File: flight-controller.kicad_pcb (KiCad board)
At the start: 2 copper layers, 35 x 43 mm, 16 parts, among them J1 USB_C_Receptacle_USB2.0_16P, SW1 SW_Push, U1 ESP32-C3-WROOM-02, U2 MPU-6050, U3 AMS1117-3.3

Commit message: Improvements to schematics and PCB design. - GND always points down - Power always points up - Adjusted powerlines
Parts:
- moved R1 1.48 mm to (208.0, 73.5)
- moved R2 1.48 mm to (208.0, 75.5)
- moved J1 1.48 mm to (200.7, 75.3)
- moved R3 0.62 mm to (178.8, 57.9), turned to 90 degrees
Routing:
- net +3.3V: track 70.7 -> 73.2 mm
- net Net-(U1-EN): track 39.6 -> 37.6 mm, vias 4 -> 2
- net +5V: track 48.0 -> 49.5 mm
- net /USB_D-: track 42.9 -> 43.6 mm
- net /USB_D+: track 42.9 -> 43.6 mm

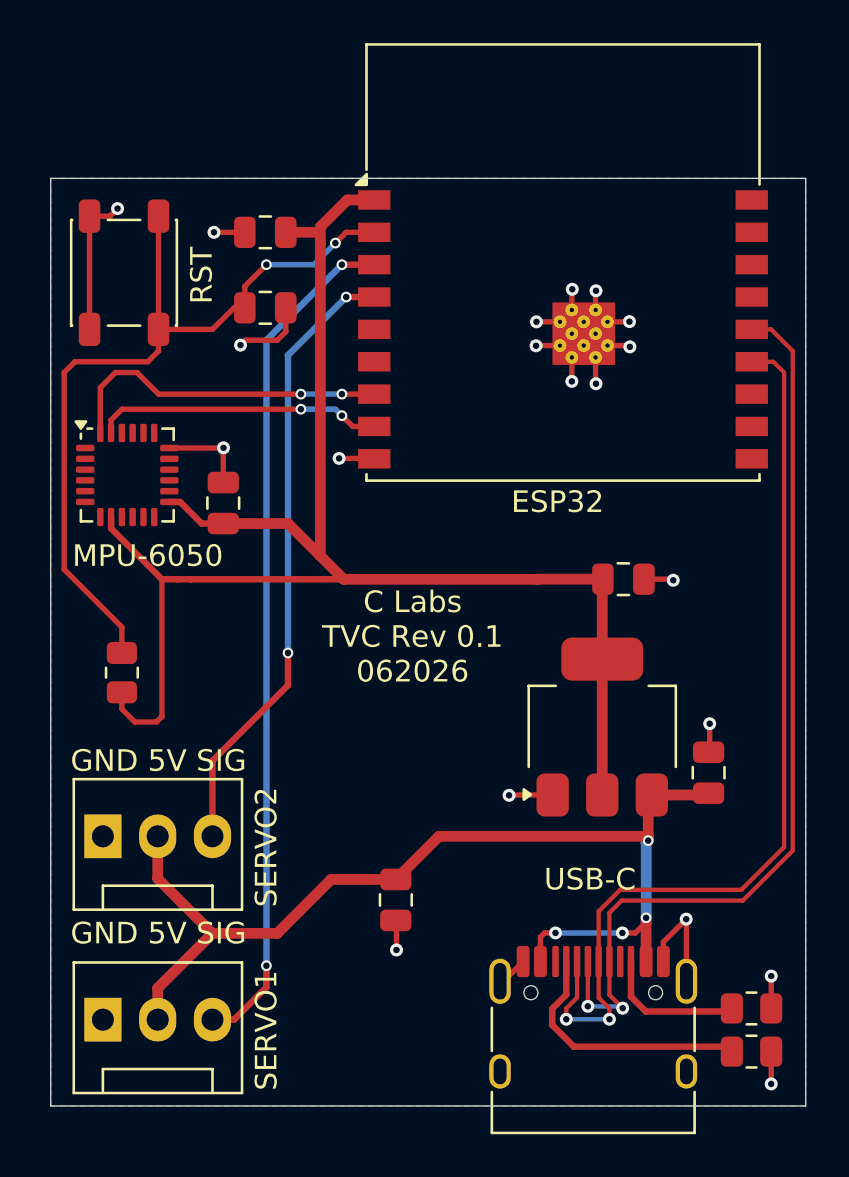
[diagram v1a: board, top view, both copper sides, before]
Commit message: Restructued Layout slightly and added new BOM
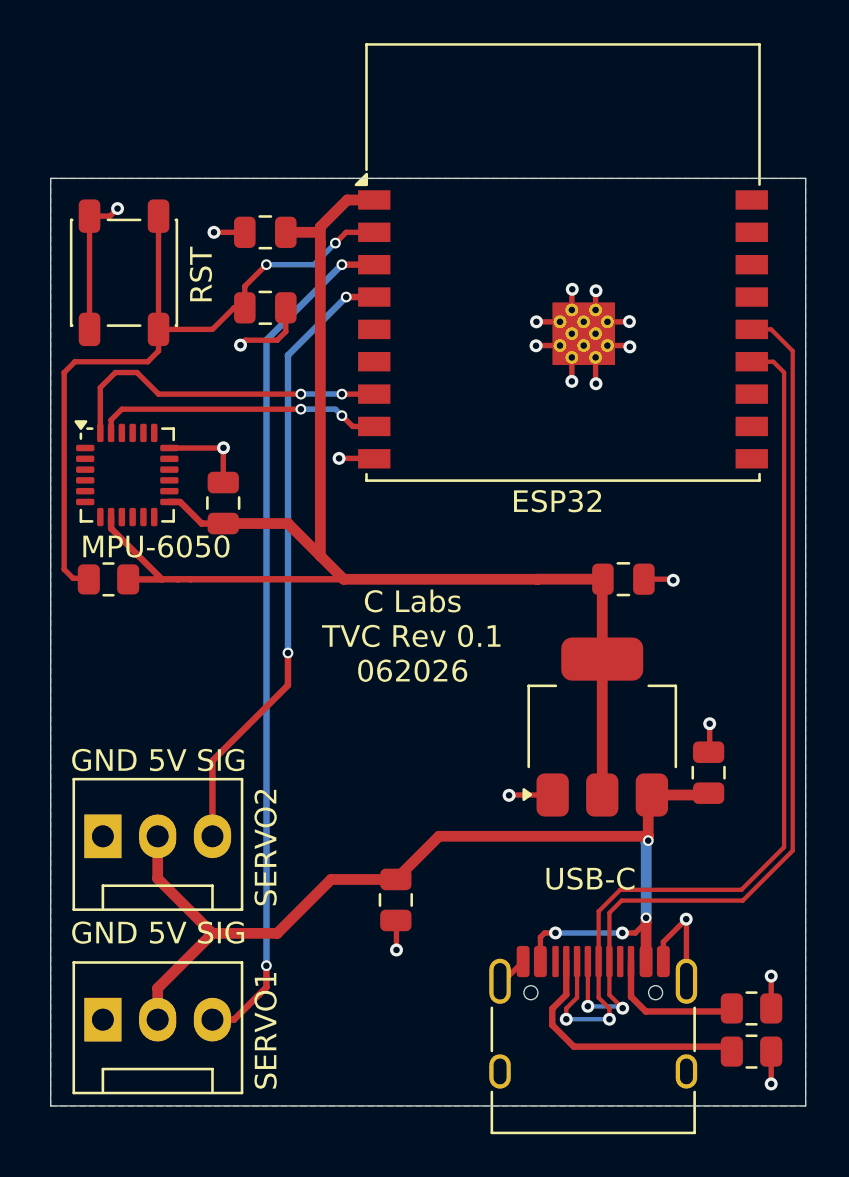
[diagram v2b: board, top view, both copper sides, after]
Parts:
- moved R3 4.37 mm to (178.2, 53.6), turned to 180 degrees
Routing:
- net +3.3V: track 73.2 -> 65.4 mm
- net Net-(U1-EN): track 37.6 -> 33.9 mm
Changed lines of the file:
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@@
 		(capping no)
 		(filling no)
-		(zone_defaults)
 		(pcbplotparams
 			(layerselection 0x00000000_00000000_55555555_5755f5ff)
@@
 		(sheetname "/")
 		(sheetfile "flight-controller.kicad_sch")
-		(units
-			(unit
-				(name "A")
-				(pins "2" "18" "17" "16" "15" "3" "4" "5" "6" "7" "8" "10" "13" "14"
-					"1" "9" "19" "11" "12"
-				)
-			)
-		)
 		(attr smd)
 		(duplicate_pad_numbers_are_jumpers no)
@@
 			(at -0.14 -0.35)
 			(size 0.6 0.6)
-			(drill 0.2)
+			(drill 0.3)
 			(property pad_prop_heatsink)
 			(layers "*.Cu" "F.Mask")
@@
 			(at -0.14 0.75)
 			(size 0.6 0.6)
-			(drill 0.2)
+			(drill 0.3)
 			(property pad_prop_heatsink)
 			(layers "*.Cu" "F.Mask")
@@
 			(at 0.41 -0.9)
 			(size 0.6 0.6)
-			(drill 0.2)
+			(drill 0.3)
 			(property pad_prop_heatsink)
 			(layers "*.Cu" "F.Mask")
@@
 			(at 0.41 0.2)
 			(size 0.6 0.6)
-			(drill 0.2)
+			(drill 0.3)
 			(property pad_prop_heatsink)
 			(layers "*.Cu" "F.Mask")
@@
 			(at 0.41 1.3)
 			(size 0.6 0.6)
-			(drill 0.2)
+			(drill 0.3)
 			(property pad_prop_heatsink)
 			(layers "*.Cu" "F.Mask")
@@
 			(at 0.96 -0.35)
 			(size 0.6 0.6)
-			(drill 0.2)
+			(drill 0.3)
 			(property pad_prop_heatsink)
 			(layers "*.Cu" "F.Mask")
@@
 			(at 0.96 0.75)
 			(size 0.6 0.6)
-			(drill 0.2)
+			(drill 0.3)
 			(property pad_prop_heatsink)
 			(layers "*.Cu" "F.Mask")
@@
 			(at 1.51 -0.9)
 			(size 0.6 0.6)
-			(drill 0.2)
+			(drill 0.3)
 			(property pad_prop_heatsink)
 			(layers "*.Cu" "F.Mask")
@@
 			(at 1.51 0.2)
 			(size 0.6 0.6)
-			(drill 0.2)
+			(drill 0.3)
 			(property pad_prop_heatsink)
 			(layers "*.Cu" "F.Mask")
@@
 			(at 1.51 1.3)
 			(size 0.6 0.6)
-			(drill 0.2)
+			(drill 0.3)
 			(property pad_prop_heatsink)
 			(layers "*.Cu" "F.Mask")
@@
 			(at 2.06 -0.35)
 			(size 0.6 0.6)
-			(drill 0.2)
+			(drill 0.3)
 			(property pad_prop_heatsink)
 			(layers "*.Cu" "F.Mask")
@@
 			(at 2.06 0.75)
 			(size 0.6 0.6)
-			(drill 0.2)
+			(drill 0.3)
 			(property pad_prop_heatsink)
 			(layers "*.Cu" "F.Mask")
@@
 	(footprint "Resistor_SMD:R_0805_2012Metric"
 		(layer "F.Cu")
-		(at 178.8 57.9125 90)
+		(at 178.18 53.59 180)
 		(descr "Resistor SMD 0805 (2012 Metric), square (rectangular) end terminal, IPC-7351 nominal, (Body size source: IPC-SM-782 page 72, https://www.pcb-3d.com/wordpress/wp-content/uploads/ipc-sm-782a_amendment_1_and_2.pdf)")
 		(tags "resistor")
 		(property "Reference" "R3"
-			(at 0 -1.65 90)
+			(at 0 -1.65 0)
 			(layer "F.SilkS")
 			(hide yes)
@@
 		)
 		(property "Value" "10k"
-			(at 0 1.65 90)
+			(at 0 1.65 0)
 			(layer "F.Fab")
 			(hide yes)
@@
 		)
 		(property "Datasheet" ""
-			(at 0 0 90)
+			(at 0 0 0)
 			(layer "F.Fab")
 			(hide yes)
@@
 		)
 		(property "Description" "Resistor"
-			(at 0 0 90)
+			(at 0 0 0)
 			(layer "F.Fab")
 			(hide yes)
@@
 		)
 		(property "KiLib_Generator" "SMD_2terminal_chip_molded"
-			(at 0 0 90)
+			(at 0 0 0)
 			(layer "F.SilkS")
 			(hide yes)
@@
 		(duplicate_pad_numbers_are_jumpers no)
 		(fp_line
-			(start -0.227064 -0.735)
-			(end 0.227064 -0.735)
+			(start -0.227064 0.735)
+			(end 0.227064 0.735)
 			(stroke
 				(width 0.12)
@@
 		)
 		(fp_line
-			(start -0.227064 0.735)
-			(end 0.227064 0.735)
+			(start -0.227064 -0.735)
+			(end 0.227064 -0.735)
 			(stroke
 				(width 0.12)
@@
 		)
 		(fp_text user "${REFERENCE}"
-			(at 0 0 90)
+			(at 0 0 0)
 			(layer "F.Fab")
 			(effects
@@
 		)
 		(fp_text user "${REFERENCE}"
-			(at 0 0 90)
+			(at 0 0 0)
 			(layer "F.Fab")
 			(effects
@@
 		)
 		(pad "1" smd roundrect
-			(at -0.9125 0 90)
+			(at -0.9125 0 180)
 			(size 1.025 1.4)
 			(layers "F.Cu" "F.Mask" "F.Paste")
@@
 		)
 		(pad "2" smd roundrect
-			(at 0.9125 0 90)
+			(at 0.9125 0 180)
 			(size 1.025 1.4)
 			(layers "F.Cu" "F.Mask" "F.Paste")
@@
 	)
 	(gr_text "MPU-6050\n"
-		(at 180 52.5 0)
+		(at 180.38 52.1 0)
 		(layer "F.SilkS")
 		(effects
@@
 	)
 	(segment
+		(start 180.65188 53.59)
+		(end 180.65688 53.585)
+		(width 0.25)
+		(layer "F.Cu")
+		(net "+3.3V")
+	)
+	(segment
 		(start 201.07 57.285)
 		(end 201.07 53.61)
@@
 	)
 	(segment
+		(start 179.0925 53.59)
+		(end 180.65188 53.59)
+		(width 0.3)
+		(layer "F.Cu")
+		(net "+3.3V")
+	)
+	(segment
 		(start 189.25 36)
 		(end 190.5 36)
@@
 	)
 	(segment
-		(start 180.4 60.2)
-		(end 179.4 60.2)
-		(width 0.25)
-		(layer "F.Cu")
-		(net "+3.3V")
-	)
-	(segment
 		(start 198.07 53.585)
 		(end 189.085 53.585)
@@
 	)
 	(segment
-		(start 178.8 59.6)
-		(end 178.8 58.825)
-		(width 0.25)
-		(layer "F.Cu")
-		(net "+3.3V")
-	)
-	(segment
 		(start 180.65688 53.585)
 		(end 181.4 53.585)
@@
 	)
 	(segment
-		(start 179.4 60.2)
-		(end 178.8 59.6)
-		(width 0.25)
-		(layer "F.Cu")
-		(net "+3.3V")
-	)
-	(segment
 		(start 182.5 51)
 		(end 183.5 51)
@@
 	)
 	(segment
-		(start 180.65688 53.585)
-		(end 180.65688 59.94312)
-		(width 0.25)
-		(layer "F.Cu")
-		(net "+3.3V")
-	)
-	(segment
 		(start 198.075 53.58)
 		(end 201.1 53.58)
@@
 	)
 	(segment
-		(start 180.65688 59.94312)
-		(end 180.4 60.2)
-		(width 0.25)
-		(layer "F.Cu")
-		(net "+3.3V")
-	)
-	(segment
 		(start 183.5 51)
 		(end 186.5 51)
@@
 	)
 	(segment
-		(start 178.8 55.8)
-		(end 178.8 57)
-		(width 0.25)
-		(layer "F.Cu")
-		(net "Net-(U1-EN)")
-	)
-	(segment
-		(start 176.125 53.125)
-		(end 178.8 55.8)
+		(start 176.54 53.54)
+		(end 177.2675 53.54)
 		(width 0.25)
 		(layer "F.Cu")
@@
 		(width 0.25)
 		(layer "F.Cu")
+		(net "Net-(U1-EN)")
+	)
+	(segment
+		(start 176.125 53.125)
+		(end 176.54 53.54)
+		(width 0.25)
+		(layer "F.Cu")

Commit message: Redone the layout of the PCB to incorporate the Power LED and Status LED Also removed MPU6050 and replaced with IMC 20602 and relevant capacitors Added 2 pull up resistors to SCL and SDA lines
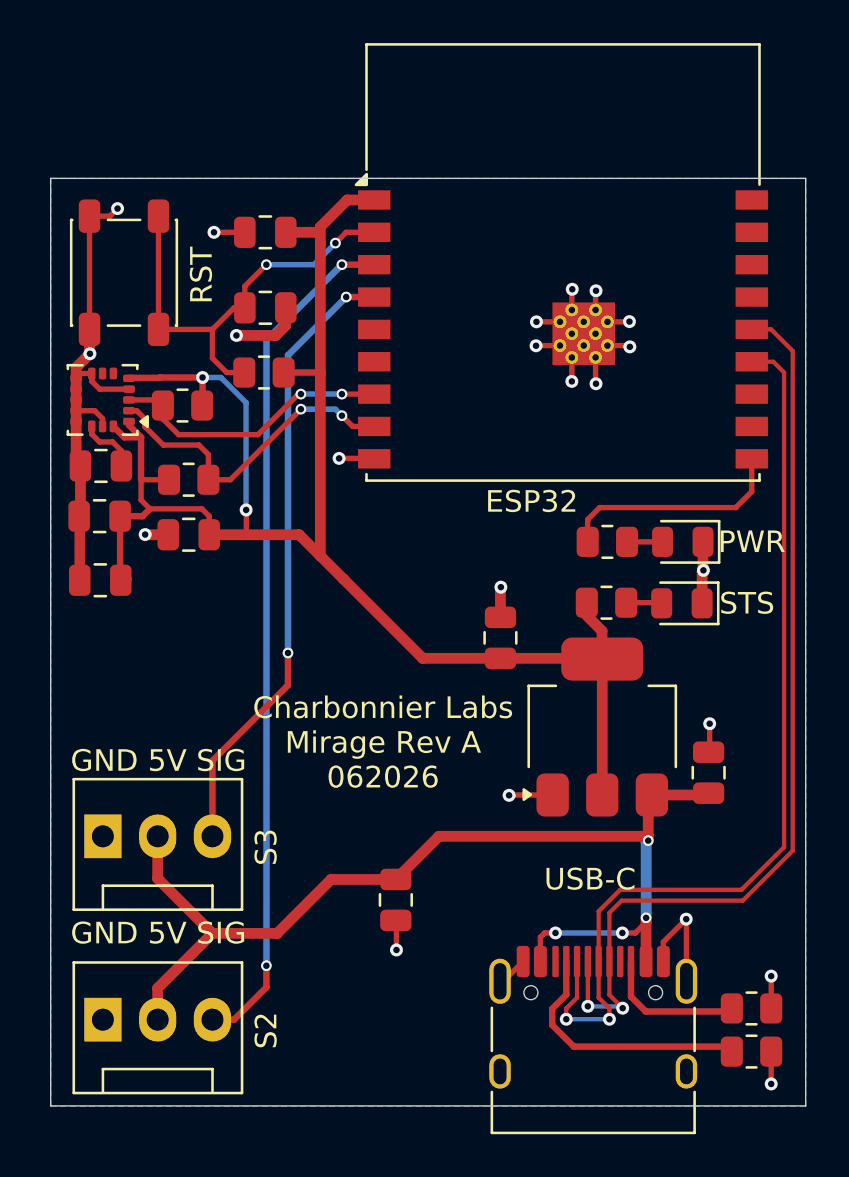
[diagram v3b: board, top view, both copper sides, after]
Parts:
- removed U2: MPU-6050, Sensor_Motion:InvenSense_QFN-24_4x4mm_P0.5mm
- added C7: 2.2µF, Capacitor_SMD:C_0805_2012Metric, F.Cu at (177.8, 50.7)
- added C8: 100nF, Capacitor_SMD:C_0805_2012Metric, F.Cu at (177.8, 53.6)
- added C9: 10nF, Capacitor_SMD:C_0805_2012Metric, F.Cu at (181.9, 51.5)
- added PWR: LED, LED_SMD:LED_0805_2012Metric, F.Cu at (204.8, 51.9)
- added R4: 1k, Resistor_SMD:R_0805_2012Metric, F.Cu at (201.3, 54.7)
- added R5: 1k, Resistor_SMD:R_0805_2012Metric, F.Cu at (201.3, 51.9)
- added R6: 4.7k, Resistor_SMD:R_0805_2012Metric, F.Cu at (181.6, 45.5)
- added R7: 4.7k, Resistor_SMD:R_0805_2012Metric, F.Cu at (181.9, 49.0)
- added STS: LED, LED_SMD:LED_0805_2012Metric, F.Cu at (204.8, 54.7)
- added U4: ICM-20602, Package_LGA:LGA-16_3x3mm_P0.5mm_LayoutBorder3x5y, F.Cu at (177.9, 45.3)
- moved R3 12.0 mm to (185.4, 44.0)
- moved C2 6.32 mm to (196.3, 56.3), turned to 90 degrees
- moved C4 5.93 mm to (177.8, 48.3), turned to 0 degrees
- renumbered SERVO1 to S2, SERVO2 to S3
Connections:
- C4 pad 1: +3.3V -> GND
- C4 pad 2: GND -> Net-(U4-REGOUT)
- U1 pad 10: unconnected-(U1-IO10-Pad10) -> /STAT_LED
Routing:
- net GND: track 41.7 -> 58.4 mm, vias 20 -> 22
- net +3.3V: track 65.4 -> 80.4 mm, vias 0 -> 2
- net Net-(U1-EN): track 33.9 -> 20.8 mm
- net /STAT_LED: track 0.00 -> 10.7 mm
- net Net-(U4-REGOUT): track 0.00 -> 2.76 mm
- net /SDA: track 15.5 -> 13.2 mm
- net /SCL: track 13.3 -> 15.3 mm
- net Net-(D1-A): track 0.00 -> 1.66 mm
- net Net-(D2-A): track 0.00 -> 1.65 mm
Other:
- board text added: "Charbonnier Labs Mirage Rev A 062026"
- board text removed: "C Labs TVC Rev 0.1 062026"
- board text removed: "MPU-6050"
